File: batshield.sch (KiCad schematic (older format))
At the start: 69 parts, among them J1 I/O 1, J2 arduinoUnoPinout, J3 mic in, J4 I/O 1, J5 mic in, J6 Audio-Jack-2, J7 Audio-Jack-2, J8 DIN-5_180degree, J9 DIN-5_180degree, Q1 2N3904, SW1 RESET, SW10 SW_SPST, SW11 SW_Push, SW12 SW_Push, SW13 SW_Push, SW2 SOFT/HARD SERIAL READ, SW3 SOFT/HARD SERIAL WRITE, SW4 RUN/PROG, SW5 HIFI/LOFI, SW6 PWM/FILTERED, SW7 NORMAL/BRIGHT, SW8 SW_SPST, SW9 SW_SPST, U1 TL072, U2 6N138

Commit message: pcb pasando drc
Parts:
- removed J3, J5: mic in, symbol Audio-Jack-2
- removed J6, J7: Audio-Jack-2, symbol Audio-Jack-2
- removed U1: TL072, symbol TL072
- added J2, J5: mic in 1/4'', conectores:Jack_Female_6,35mm_HD, symbol Audio-Jack-3_3Switches
- added U1: TL062, Housings_DIP:DIP-8_W7.62mm, symbol TL062
- C10, C11, C5, C6, C8, C9: footprint (none) -> Capacitors_THT:C_Disc_D5.0mm_W2.5mm_P5.00mm
- C2, C4: footprint (none) -> Capacitors_THT:CP_Radial_D5.0mm_P2.50mm
- D1: value 1N4004 -> 1N4148; footprint (none) -> Diodes_THT:D_DO-35_SOD27_P7.62mm_Horizontal
- J1: footprint (none) -> Pin_Headers:Pin_Header_Straight_1x03_Pitch2.54mm
- J3: renamed from J2; footprint (none) -> arduino:arduinoUnoPinout
- J4: value I/O 1 -> I/O 2; footprint (none) -> Pin_Headers:Pin_Header_Straight_1x03_Pitch2.54mm
- J6: renamed from J8; value DIN-5_180degree -> MIDI out; footprint (none) -> conectores:MIDI_female_5_pins
- J7: renamed from J9; value DIN-5_180degree -> MIDI IN; footprint (none) -> conectores:MIDI_female_5_pins
- Q1: footprint TO_SOT_Packages_THT:TO-92_Molded_Narrow -> TO_SOT_Packages_THT:TO-92_Inline_Wide
- R1, R10, R11, R12, R13, R14, R15, R16, R17, R18, R19, R2, R20, R21, R22, R23, R24, R25, R26, R3, R4, R5, R6, R7, R8, R9: footprint (none) -> Resistors_THT:R_Axial_DIN0207_L6.3mm_D2.5mm_P7.62mm_Horizontal
- RV1, RV2, RV3, RV4, RV5, RV6: footprint (none) -> conectores:potenciometro_PTV09
- SW1: footprint (none) -> conectores:pulsador_spst_mini
- SW10: value SW_SPST -> SWT3; footprint (none) -> conectores:interruptor_spdt
- SW11: value SW_Push -> BTN1; footprint (none) -> conectores:button_spst
- SW12: value SW_Push -> BTN2; footprint (none) -> conectores:button_spst
- SW13: value SW_Push -> BTN3; footprint (none) -> conectores:button_spst
- SW2: value SOFT/HARD SERIAL READ -> SW/HW SER R; footprint (none) -> conectores:interruptor_spdt
- SW3: value SOFT/HARD SERIAL WRITE -> SW/HW SER W; footprint (none) -> conectores:interruptor_spdt
- SW4, SW5, SW6, SW7: footprint (none) -> conectores:interruptor_spdt
- SW8: value SW_SPST -> SWT1; footprint (none) -> conectores:interruptor_spdt
- SW9: value SW_SPST -> SWT2; footprint (none) -> conectores:interruptor_spdt
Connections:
- net +5V: now also U1.8 (V+)
- net BTN1: now also J3.21 (D7); no longer J3.18 (D4)
- net BTN3: now also J3.18 (D4); no longer J3.21 (D7)
- net GND: now also J2.2, J5.2, U1.4 (V-)
- net SWT1: now also J3.27 (D13); no longer J3.22 (D8)
- net SWT3: now also J3.22 (D8); no longer J3.27 (D13)
- net at C10.1, C7.1, R10.1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: now also J5.1
- net at C3.2, R7.1: now also J2.1
- net at C1.1, R2.1, R4.2: now also U1.1
- net at C1.2, R2.2, RV1.2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: now also U1.2 (-)
- net at C6.1, R5.1: now also U1.3 (+)
- no-connect marks 10 -> 18
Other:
- note removed: "jack 1/4''"
- note removed: "jack 1/8''"

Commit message: añado algunos modelos 3d
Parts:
- C3: footprint Capacitors_THT:C_Disc_D5.0mm_W2.5mm_P2.50mm -> Capacitors_THT:C_Disc_D5.0mm_W2.5mm_P5.00mm
- SW1: footprint conectores:pulsador_spst_mini -> Buttons_Switches_THT:SW_PUSH_6mm_h5mm
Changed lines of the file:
@@
 LIBS:optoacopladores
 LIBS:conectores
+LIBS:batshield-cache
 EELAYER 25 0
 EELAYER END
@@
 F 0 "C3" H 1775 2050 50  0000 L CNN
 F 1 "0.1u" H 1775 1850 50  0000 L CNN
-F 2 "Capacitors_THT:C_Disc_D5.0mm_W2.5mm_P2.50mm" H 1788 1800 50  0001 C CNN
+F 2 "Capacitors_THT:C_Disc_D5.0mm_W2.5mm_P5.00mm" H 1788 1800 50  0001 C CNN
 F 3 "" H 1750 1950 50  0001 C CNN
 	1    1750 1950
@@
 F 0 "SW1" H 6100 1250 50  0000 L CNN
 F 1 "RESET" H 6050 1090 50  0000 C CNN
-F 2 "conectores:pulsador_spst_mini" H 6050 1350 50  0001 C CNN
+F 2 "Buttons_Switches_THT:SW_PUSH_6mm_h5mm" H 6050 1350 50  0001 C CNN
 F 3 "" H 6050 1350 50  0001 C CNN
 	1    6050 1150

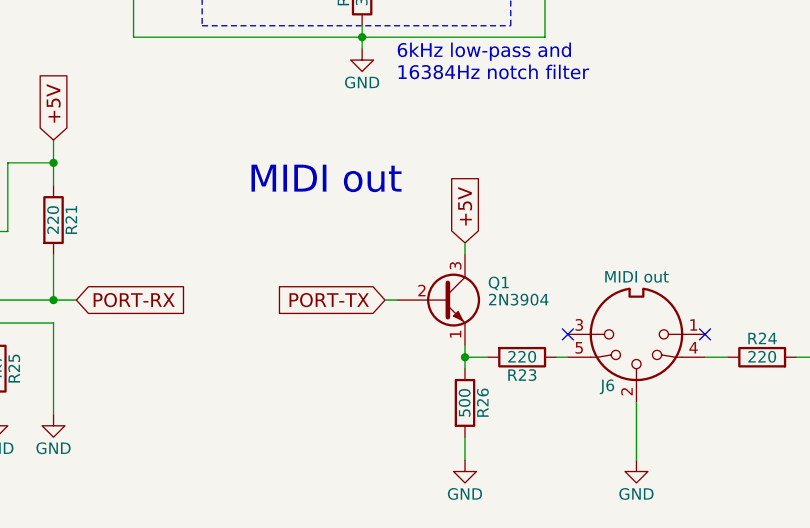
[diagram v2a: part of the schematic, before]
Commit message: quito transistor del circuito midi out
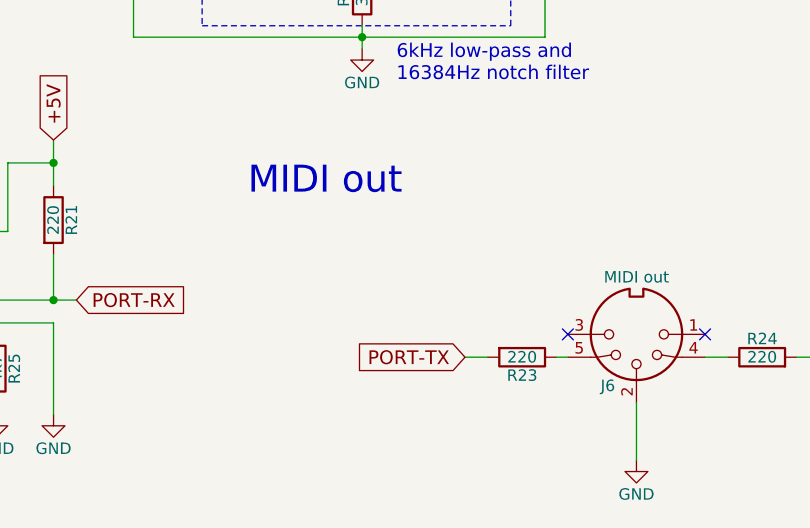
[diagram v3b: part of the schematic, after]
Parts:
- removed Q1: 2N3904, TO_SOT_Packages_THT:TO-92_Inline_Wide, symbol 2N3904
- removed R26: 500, Resistors_THT:R_Axial_DIN0207_L6.3mm_D2.5mm_P7.62mm_Horizontal, symbol R
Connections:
- net PORT-TX: now also R23.2
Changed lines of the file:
@@
 Text GLabel 6300 6950 2    60   Input ~ 0
 +5V
-Text GLabel 4400 6700 0    60   Input ~ 0
+Text GLabel 4750 6950 0    60   Input ~ 0
 PORT-TX
 Text Notes 3800 6250 0    118  ~ 0
@@
 	1    0    0    -1
 $EndComp
-$Comp
-L 2N3904 Q1
-U 1 1 5A0D692E
-P 4650 6700
-F 0 "Q1" H 4850 6775 50  0000 L CNN
-F 1 "2N3904" H 4850 6700 50  0000 L CNN
-F 2 "TO_SOT_Packages_THT:TO-92_Inline_Wide" H 4850 6625 50  0001 L CIN
-F 3 "" H 4650 6700 50  0001 L CNN
-	1    4650 6700
-	1    0    0    -1
-$EndComp
-$Comp
-L R R26
-U 1 1 5A0D6A1C
-P 4750 7150
-F 0 "R26" V 4830 7150 50  0000 C CNN
-F 1 "500" V 4750 7150 50  0000 C CNN
-F 2 "Resistors_THT:R_Axial_DIN0207_L6.3mm_D2.5mm_P7.62mm_Horizontal" V 4680 7150 50  0001 C CNN
-F 3 "" H 4750 7150 50  0001 C CNN
-	1    4750 7150
-	1    0    0    -1
-$EndComp
-$Comp
-L GND #PWR024
-U 1 1 5A0D6B0A
-P 4750 7400
-F 0 "#PWR024" H 4750 7150 50  0001 C CNN
-F 1 "GND" H 4750 7250 50  0000 C CNN
-F 2 "" H 4750 7400 50  0001 C CNN
-F 3 "" H 4750 7400 50  0001 C CNN
-	1    4750 7400
-	1    0    0    -1
-$EndComp
-Text GLabel 4750 6450 1    60   Input ~ 0
-+5V
 $Comp
 L 6N138 U2
@@
 Connection ~ 4850 1950
 Wire Wire Line
-	4750 6900 4750 7000
-Wire Wire Line
-	4750 7300 4750 7400
-Wire Wire Line
-	4400 6700 4450 6700
-Wire Wire Line
 	5500 7150 5500 7400
-Connection ~ 4750 6950
-Wire Wire Line
-	4850 6950 4750 6950
 Wire Wire Line
 	5200 6950 5150 6950
@@
 Wire Wire Line
 	6200 6950 6300 6950
-Wire Wire Line
-	4750 6500 4750 6450
 Wire Wire Line
 	2650 6400 2750 6400
@@
 NoConn ~ 5300 4500
 NoConn ~ 5300 4700
+Wire Wire Line
+	4750 6950 4850 6950
 $EndSCHEMATC
